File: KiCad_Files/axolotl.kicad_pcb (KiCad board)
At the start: 2 copper layers, 89.7 x 49.4 mm, 8 parts, among them SW1 SW_DIP_x01

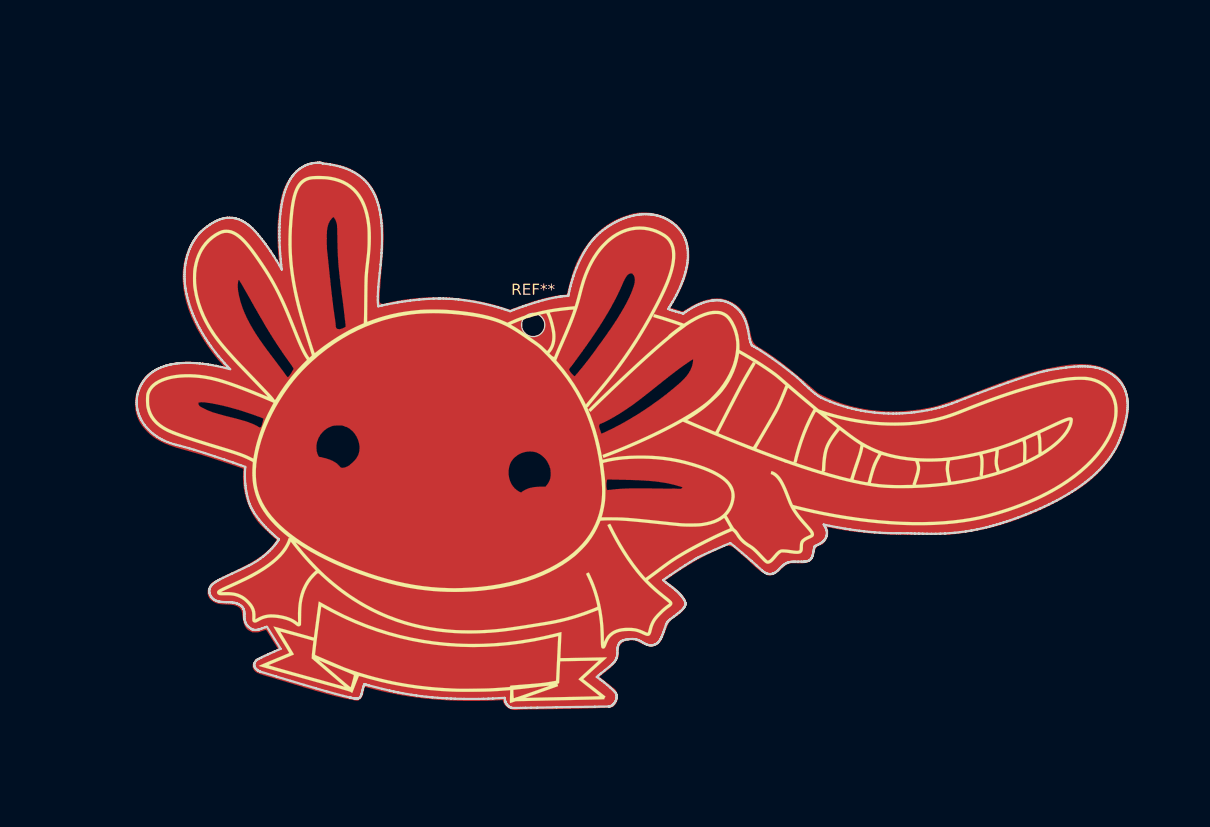
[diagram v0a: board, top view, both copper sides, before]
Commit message: modifed pcb and updtaed tracks, footprints and fill-zones
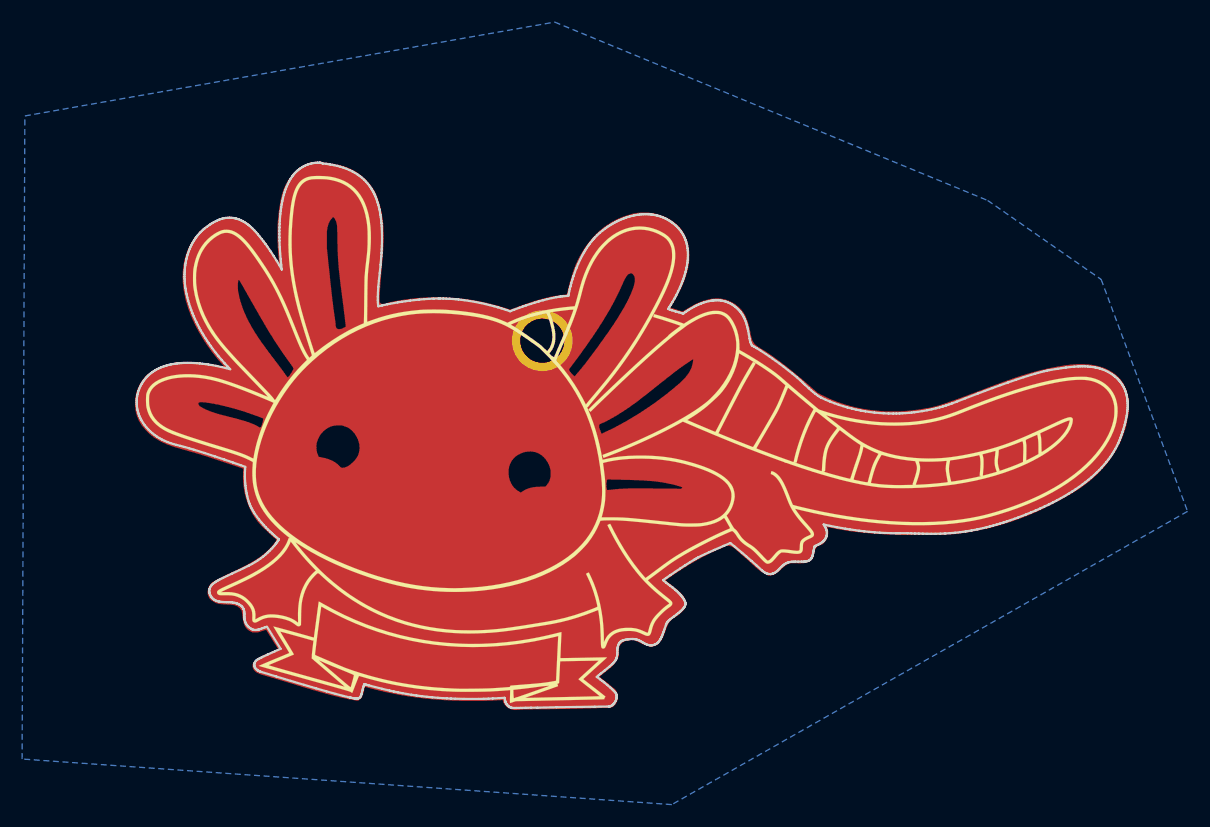
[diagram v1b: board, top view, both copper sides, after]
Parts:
- moved REF** 1.65 mm to (109.2, 50.6)
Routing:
- net GND: track 60.0 -> 0.00 mm
- net +3V0: track 54.0 -> 48.2 mm
- net VCC: track 89.1 -> 90.4 mm
- added copper zone on B.Cu, net GND
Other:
- board text added: "Axolotl"
- board text added: "v1.1"
- board text removed: "Axo"
- board text removed: "v1.0"
